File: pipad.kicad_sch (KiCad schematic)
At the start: 4 parts

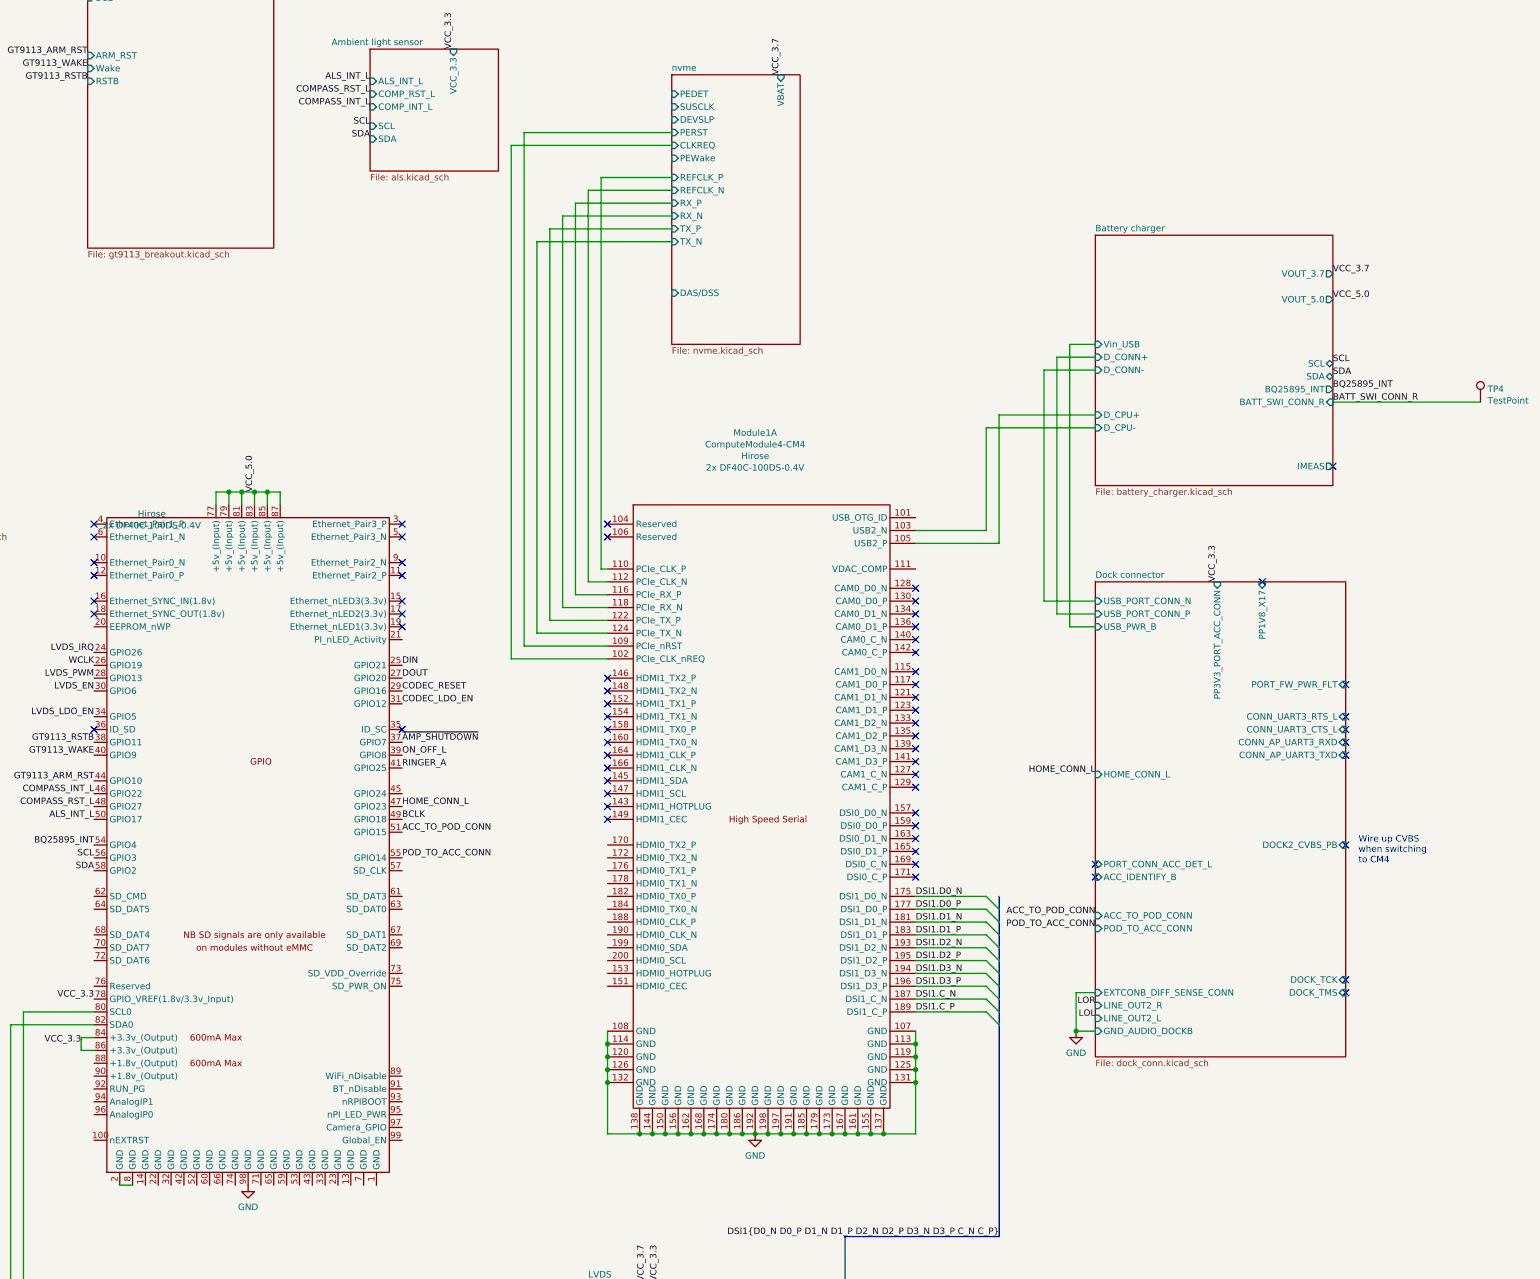
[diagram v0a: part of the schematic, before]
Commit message: Add buck-boost regulator for PCIe 3.3V
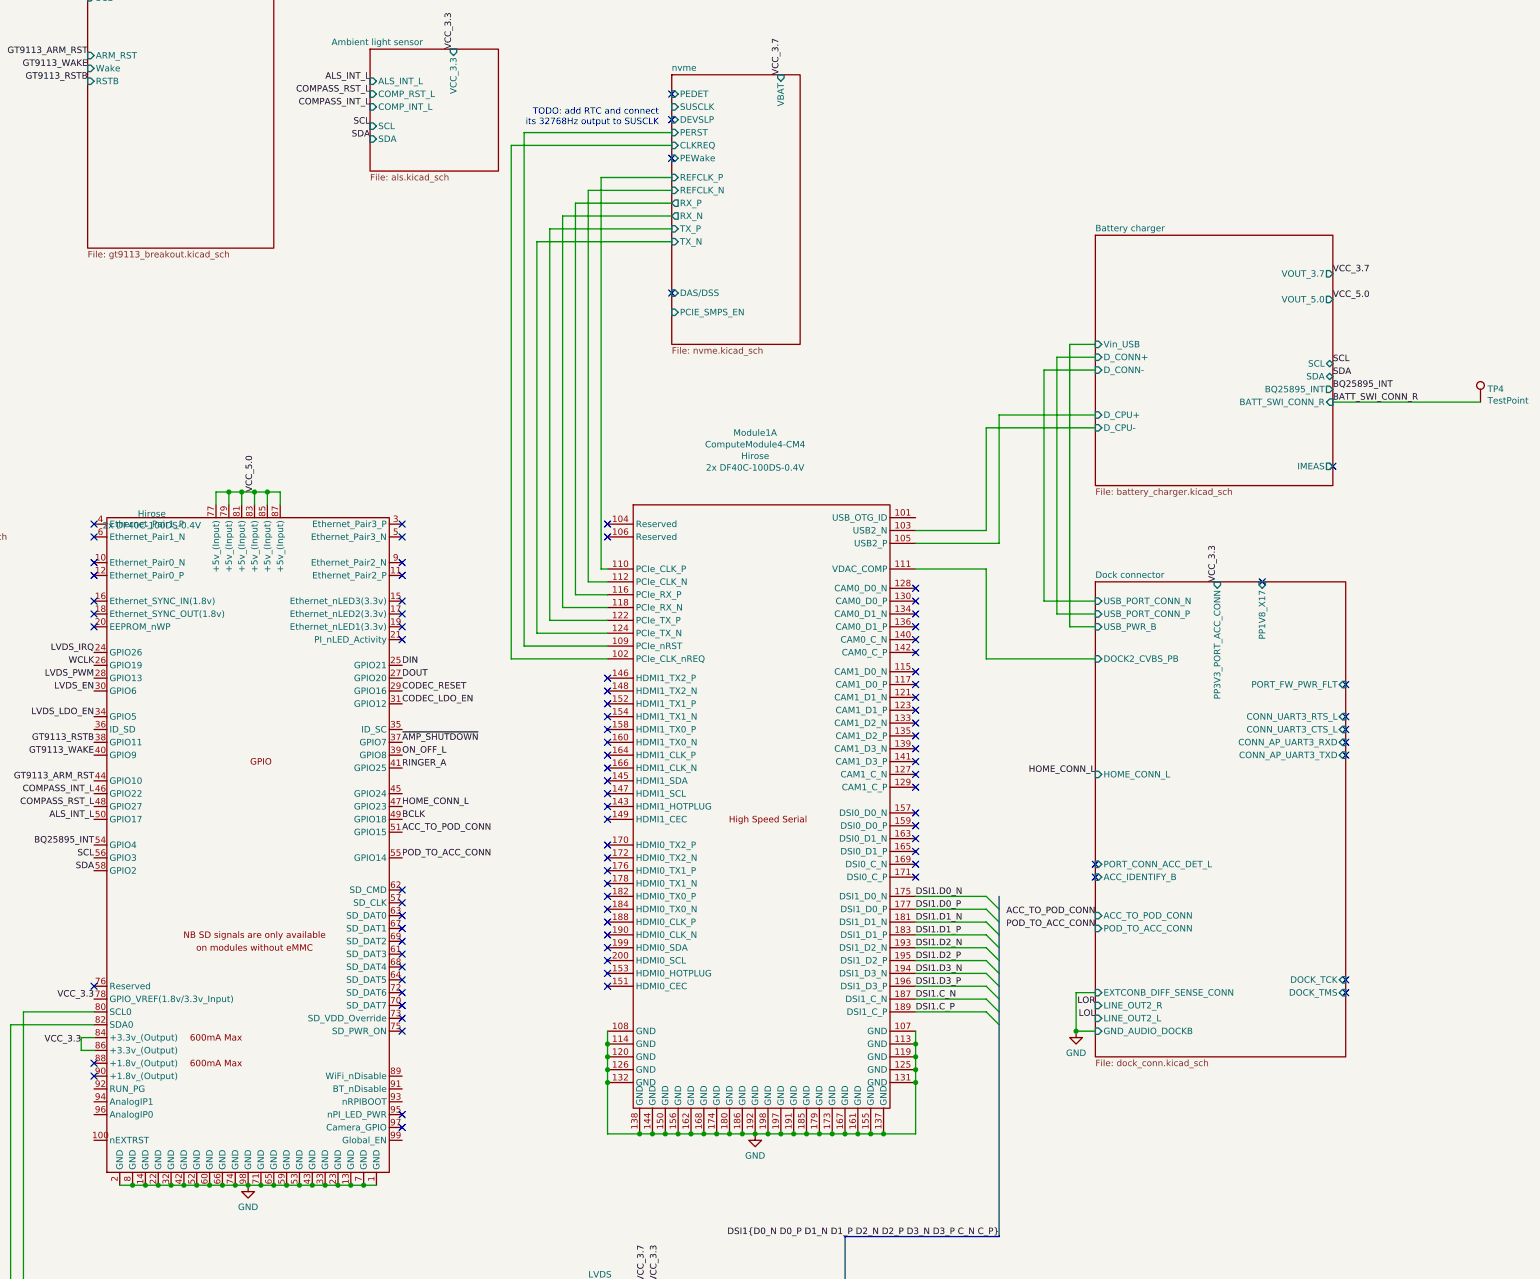
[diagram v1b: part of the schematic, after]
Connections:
- net Dock connector/DOCK2_CVBS_PB: now also Module1.111 (VDAC_COMP)
- net GND: now also Module1.1 (GND), Module1.13 (GND), Module1.14 (GND), Module1.2 (GND), Module1.22 (GND), Module1.23 (GND), Module1.32 (GND), Module1.33 (GND), Module1.42 (GND), Module1.43 (GND), Module1.52 (GND), Module1.53 (GND), Module1.59 (GND), Module1.60 (GND), Module1.65 (GND), Module1.66 (GND), Module1.7 (GND), Module1.71 (GND), Module1.74 (GND), Module1.8 (GND)
- no-connect marks 63 -> 95
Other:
- sheet nvme ports: added PCIE_SMPS_EN; removed none
- note added: "TODO: add RTC and connect its 32768Hz output to SUSCLK"
- note removed: "Wire up CVBS when switching to CM4"

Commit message: Route CM4 board with differential connector on the right.
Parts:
- removed R25, R26: 10k, Resistor_SMD:R_0402_1005Metric, symbol Device:R
- removed TP4: TestPoint, TestPoint:TestPoint_THTPad_1.0x1.0mm_Drill0.5mm, symbol Connector:TestPoint
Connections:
- net ON_OFF_L: no longer Module1.39 (GPIO8)
- net nEXTRST: now reaches Module1.100 (nEXTRST)
- net VOL_DN_L: now reaches Module1.45 (GPIO24)
- net ~AMP_SHUTDOWN renamed VOL_UP_L
- new net ~{PWR_BUTTON_INT}: Module1.39 (GPIO8)
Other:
- sheet Battery charger ports: added ~{PB_IN}, ~{PWR_BUTTON_INT}, ~{PWR_CLR}; removed none
- sheet codec and amp ports: added DOUT_TERM, ~{AMP_SHUTDOWN}, ~{CODEC_RESET}; removed DOUT, ~AMP_SHUTDOWN, ~CODEC_RESET

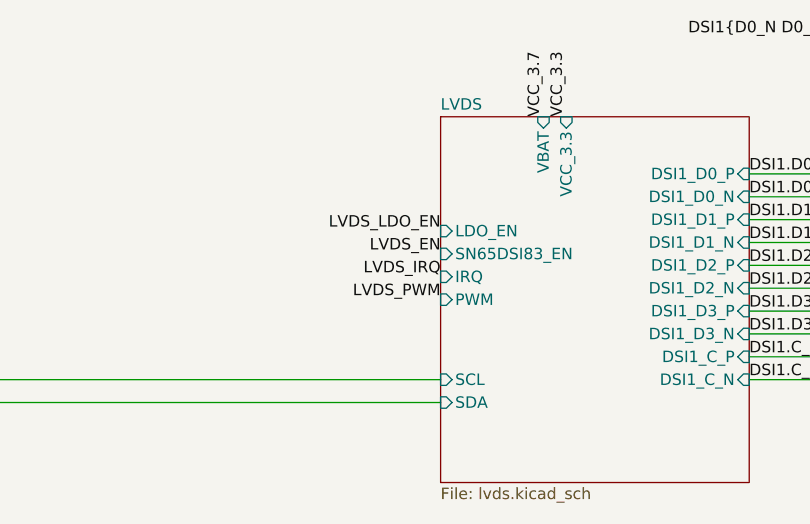
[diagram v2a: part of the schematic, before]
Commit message: Switch tps61176 for tps61177, since 61176 is out of stock. Also finish fixing hole clearance violations.
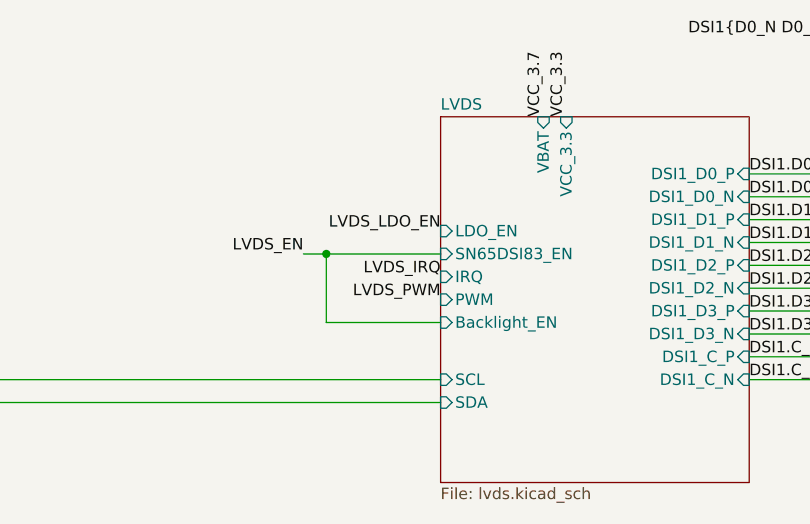
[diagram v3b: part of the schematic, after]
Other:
- sheet LVDS ports: added Backlight_EN; removed none
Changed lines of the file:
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@@
   (junction (at 349.25 248.92) (diameter 1.016) (color 0 0 0 0)
+  )
+  (junction (at 240.03 313.69) (diameter 0) (color 0 0 0 0)
   )
   (junction (at 303.53 269.24) (diameter 1.016) (color 0 0 0 0)
@@
     (stroke (width 0) (type solid) (color 0 0 0 0))
   )
+  (wire (pts (xy 252.73 321.31) (xy 240.03 321.31))
+    (stroke (width 0) (type default) (color 0 0 0 0))
+  )
   (bus (pts (xy 334.01 245.11) (xy 334.01 247.65))
     (stroke (width 0) (type solid) (color 0 0 0 0))
@@
     (stroke (width 0) (type solid) (color 0 0 0 0))
   )
+  (wire (pts (xy 237.49 313.69) (xy 240.03 313.69))
+    (stroke (width 0) (type default) (color 0 0 0 0))
+  )
   (wire (pts (xy 140.97 245.11) (xy 154.94 245.11))
     (stroke (width 0) (type solid) (color 0 0 0 0))
@@
     (stroke (width 0) (type solid) (color 0 0 0 0))
   )
+  (wire (pts (xy 240.03 321.31) (xy 240.03 313.69))
+    (stroke (width 0) (type default) (color 0 0 0 0))
+  )
   (bus (pts (xy 303.53 320.04) (xy 303.53 322.58))
     (stroke (width 0) (type solid) (color 0 0 0 0))
+  )
+  (wire (pts (xy 240.03 313.69) (xy 252.73 313.69))
+    (stroke (width 0) (type default) (color 0 0 0 0))
   )
   (wire (pts (xy 317.5 222.25) (xy 331.47 222.25))
@@
     (effects (font (size 1.27 1.27)) (justify right bottom))
   )
-  (label "LVDS_EN" (at 252.73 313.69 180)
+  (label "LVDS_EN" (at 237.49 313.69 180)
     (effects (font (size 1.27 1.27)) (justify right bottom))
   )
@@
       (effects (font (size 1.27 1.27)) (justify right))
     )
+    (pin "Backlight_EN" input (at 252.73 321.31 180)
+      (effects (font (size 1.27 1.27)) (justify left))
+    )
   )
   (sheet (at 269.24 59.69) (size 25.4 53.34) (fields_autoplaced)
@@
       (reference "#PWR025") (unit 1) (value "GND") (footprint "")
     )
-    (path "/1cd8b29a-6edd-403b-84dd-3cf97c71d81a/5c9f788d-f8be-4264-9f98-9cc991b217dc"
-      (reference "#PWR026") (unit 1) (value "GND") (footprint "")
-    )
-    (path "/1cd8b29a-6edd-403b-84dd-3cf97c71d81a/52fecab1-8b85-430d-821a-5639f8a23dd6"
-      (reference "#PWR027") (unit 1) (value "GND") (footprint "")
-    )
-    (path "/1cd8b29a-6edd-403b-84dd-3cf97c71d81a/4834a7a9-cd44-4c08-9fcf-66be012ea3af"
-      (reference "#PWR028") (unit 1) (value "GND") (footprint "")
-    )
-    (path "/1cd8b29a-6edd-403b-84dd-3cf97c71d81a/2404d447-2a71-4333-80ba-6c76f251b763"
-      (reference "#PWR029") (unit 1) (value "GND") (footprint "")
-    )
-    (path "/1cd8b29a-6edd-403b-84dd-3cf97c71d81a/fda295f9-5722-4088-b9b7-2de5fa044887"
-      (reference "#PWR030") (unit 1) (value "GND") (footprint "")
-    )
-    (path "/1cd8b29a-6edd-403b-84dd-3cf97c71d81a/d7aa9119-7189-40e9-bd89-afe68e2237dd"
-      (reference "#PWR031") (unit 1) (value "GND") (footprint "")
-    )
-    (path "/1cd8b29a-6edd-403b-84dd-3cf97c71d81a/6454fd58-e4da-41e4-ac11-edf4c05e2ad3"
-      (reference "#PWR032") (unit 1) (value "GND") (footprint "")
-    )
     (path "/1cd8b29a-6edd-403b-84dd-3cf97c71d81a/87230ed2-c067-4bed-bd85-e992077f90ea"
       (reference "#PWR033") (unit 1) (value "GND") (footprint "")
@@
       (reference "#PWR034") (unit 1) (value "GND") (footprint "")
     )
-    (path "/1cd8b29a-6edd-403b-84dd-3cf97c71d81a/0661f722-766f-44a6-9d35-fcf651df4232"
-      (reference "#PWR035") (unit 1) (value "GND") (footprint "")
-    )
     (path "/cadc25a7-9e30-42e2-b605-972cd5d66842"
       (reference "#PWR036") (unit 1) (value "GND") (footprint "")
@@
       (reference "#PWR0144") (unit 1) (value "GND") (footprint "")
     )
+    (path "/1cd8b29a-6edd-403b-84dd-3cf97c71d81a/3f3bf656-03bd-4dd1-beca-d711dd5b0a6d"
+      (reference "#PWR0145") (unit 1) (value "GND") (footprint "")
+    )
+    (path "/1cd8b29a-6edd-403b-84dd-3cf97c71d81a/469c9557-18af-43bc-b1e0-eeddff7b0292"
+      (reference "#PWR0146") (unit 1) (value "GND") (footprint "")
+    )
+    (path "/1cd8b29a-6edd-403b-84dd-3cf97c71d81a/8e6dc559-4009-4f8e-86d4-8ff1aeb728fb"
+      (reference "#PWR0147") (unit 1) (value "GND") (footprint "")
+    )
+    (path "/1cd8b29a-6edd-403b-84dd-3cf97c71d81a/f9f0f738-d09a-411c-a923-2aeb6becdbb2"
+      (reference "#PWR0148") (unit 1) (value "GND") (footprint "")
+    )
+    (path "/1cd8b29a-6edd-403b-84dd-3cf97c71d81a/89125140-b3a6-414e-afa2-766835c02c1b"
+      (reference "#PWR0149") (unit 1) (value "GND") (footprint "")
+    )
     (path "/00000000-0000-0000-0000-00006026a3be/00000000-0000-0000-0000-000060271c8d"
       (reference "C1") (unit 1) (value "100nF") (footprint "Capacitor_SMD:C_0402_1005Metric")
@@
       (reference "C41") (unit 1) (value "100nF") (footprint "Capacitor_SMD:C_0402_1005Metric")
     )
-    (path "/1cd8b29a-6edd-403b-84dd-3cf97c71d81a/883bde91-7d01-40cd-8bac-556ba2d2b550"
-      (reference "C42") (unit 1) (value "1uF") (footprint "Capacitor_SMD:C_0402_1005Metric")
-    )
-    (path "/1cd8b29a-6edd-403b-84dd-3cf97c71d81a/a44a58be-109e-4f11-bb12-5b305446830c"
-      (reference "C43") (unit 1) (value "0.47uF") (footprint "Capacitor_SMD:C_0402_1005Metric")
-    )
-    (path "/1cd8b29a-6edd-403b-84dd-3cf97c71d81a/2e0ec137-0224-4b2a-b8ec-01b49fa4194d"
-      (reference "C44") (unit 1) (value "4.7uF") (footprint "Capacitor_SMD:C_0402_1005Metric")
+    (path "/1cd8b29a-6edd-403b-84dd-3cf97c71d81a/89dc1d95-9bc3-4c6e-8ed5-b1ddd80d0a5f"
+      (reference "C42") (unit 1) (value "4.7uF") (footprint "Capacitor_SMD:C_0805_2012Metric")
+    )
+    (path "/1cd8b29a-6edd-403b-84dd-3cf97c71d81a/edfb9291-bba8-4081-b180-5c9b214fdf26"
+      (reference "C43") (unit 1) (value "470nF") (footprint "Capacitor_SMD:C_0402_1005Metric")
+    )
+    (path "/1cd8b29a-6edd-403b-84dd-3cf97c71d81a/b9ad51c5-87a2-458e-85be-d7fffc81f34d"
+      (reference "C44") (unit 1) (value "C") (footprint "Capacitor_SMD:C_0402_1005Metric")
     )
     (path "/1cd8b29a-6edd-403b-84dd-3cf97c71d81a/369438df-81da-4173-90c2-ed7ac4bdbaa5"
       (reference "C45") (unit 1) (value "10uF") (footprint "Capacitor_SMD:C_0402_1005Metric")
     )
-    (path "/1cd8b29a-6edd-403b-84dd-3cf97c71d81a/0c2e18c5-09de-43ee-8f72-c0182e49c223"
-      (reference "C46") (unit 1) (value "2.2uF") (footprint "Capacitor_SMD:C_0402_1005Metric")
+    (path "/1cd8b29a-6edd-403b-84dd-3cf97c71d81a/6802b5d4-85bc-4506-b915-e3373f657648"
+      (reference "C46") (unit 1) (value "4.7uF") (footprint "Capacitor_SMD:C_0805_2012Metric")
     )
     (path "/eed4aa3c-bec9-4438-9bbd-324cd17b6734/00000000-0000-0000-0000-00005f7967cf"
@@
       (reference "C63") (unit 1) (value "22uF") (footprint "Capacitor_SMD:C_0805_2012Metric")
     )
-    (path "/1cd8b29a-6edd-403b-84dd-3cf97c71d81a/2e2bd6a2-0649-4331-8eef-bb523aed6947"
-      (reference "D1") (unit 1) (value "D_Schottky") (footprint "footprints:PMEG4010EPK_315")
+    (path "/1cd8b29a-6edd-403b-84dd-3cf97c71d81a/bf3f30b8-b3dc-46ba-be83-82e46ac5ce51"
+      (reference "D1") (unit 1) (value "D_Schottky") (footprint "footprints:sba0450q")
     )
     (path "/00000000-0000-0000-0000-00006026a3be/00000000-0000-0000-0000-000060262be3"
@@
       (reference "JP7") (unit 1) (value "Jumper_2_Bridged") (footprint "Resistor_SMD:R_0402_1005Metric")
     )
-    (path "/1cd8b29a-6edd-403b-84dd-3cf97c71d81a/e043cedd-01c1-42d0-b9c5-2811df027170"
-      (reference "L1") (unit 1) (value "4.7uH") (footprint "Inductor_SMD:L_0805_2012Metric")
+    (path "/1cd8b29a-6edd-403b-84dd-3cf97c71d81a/914507c3-ce29-4dbb-96fc-983ec662129a"
+      (reference "L1") (unit 1) (value "10uH") (footprint "footprints:LQH3NPZ100MGRL")
     )
     (path "/eed4aa3c-bec9-4438-9bbd-324cd17b6734/00000000-0000-0000-0000-00005f795446"
@@
       (reference "R14") (unit 1) (value "10k") (footprint "Resistor_SMD:R_0402_1005Metric")
     )
-    (path "/1cd8b29a-6edd-403b-84dd-3cf97c71d81a/a62c06ce-8870-4f3e-b9c3-edd7409eb43a"
-      (reference "R15") (unit 1) (value "53.6k") (footprint "Resistor_SMD:R_0402_1005Metric")
-    )
-    (path "/1cd8b29a-6edd-403b-84dd-3cf97c71d81a/50128048-9fa3-41d6-9ae7-cc8d2a068ac3"
-      (reference "R16") (unit 1) (value "1.3M") (footprint "Resistor_SMD:R_0402_1005Metric")
-    )
-    (path "/1cd8b29a-6edd-403b-84dd-3cf97c71d81a/fcaf88c6-19bc-4c01-9bde-6f4930c6b9e7"
-      (reference "R17") (unit 1) (value "1M") (footprint "Resistor_SMD:R_0402_1005Metric")
-    )
-    (path "/1cd8b29a-6edd-403b-84dd-3cf97c71d81a/235d5b23-169d-4712-bbc5-0ad97aa254f9"
-      (reference "R18") (unit 1) (value "82k") (footprint "Resistor_SMD:R_0402_1005Metric")
+    (path "/1cd8b29a-6edd-403b-84dd-3cf97c71d81a/7598669e-0bc4-4405-9509-d610c7cd9c0b"
+      (reference "R15") (unit 1) (value "10k") (footprint "Resistor_SMD:R_0402_1005Metric")
+    )
+    (path "/1cd8b29a-6edd-403b-84dd-3cf97c71d81a/8418579f-ccf0-4842-a1de-d065d7f3b19b"
+      (reference "R16") (unit 1) (value "10k") (footprint "Resistor_SMD:R_0402_1005Metric")
     )
     (path "/eed4aa3c-bec9-4438-9bbd-324cd17b6734/00000000-0000-0000-0000-00005f78f911"
@@
       (reference "U9") (unit 1) (value "GT9113") (footprint "footprints:GT9113")
     )
-    (path "/1cd8b29a-6edd-403b-84dd-3cf97c71d81a/750c7506-5992-4e4e-a322-eaf1b648d850"
-      (reference "U10") (unit 1) (value "TPS61176RTER") (footprint "footprints:TPS61176RTER")
+    (path "/1cd8b29a-6edd-403b-84dd-3cf97c71d81a/5e0b71fc-17cc-4cc6-ad38-4bfa57ad96c3"
+      (reference "U10") (unit 1) (value "TPS61177A") (footprint "footprints:tps61177a")
     )
     (path "/1cd8b29a-6edd-403b-84dd-3cf97c71d81a/82354318-2571-4a0b-8bb3-c49a37dd3cd6"
